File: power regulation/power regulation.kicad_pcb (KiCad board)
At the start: 4 copper layers, 175 x 100 mm, 90 parts, among them J1 Conn_01x02_Pin, J2 Conn_01x02_Pin, J3 Conn_01x02_Pin, M1 TO-236AB_SOT23_NEX, M2 TO-236AB_SOT23_NEX, U1 LT8640SEV_PBF, U2 LT8640SEV_PBF, U3 LT8619EDD-TRPBF

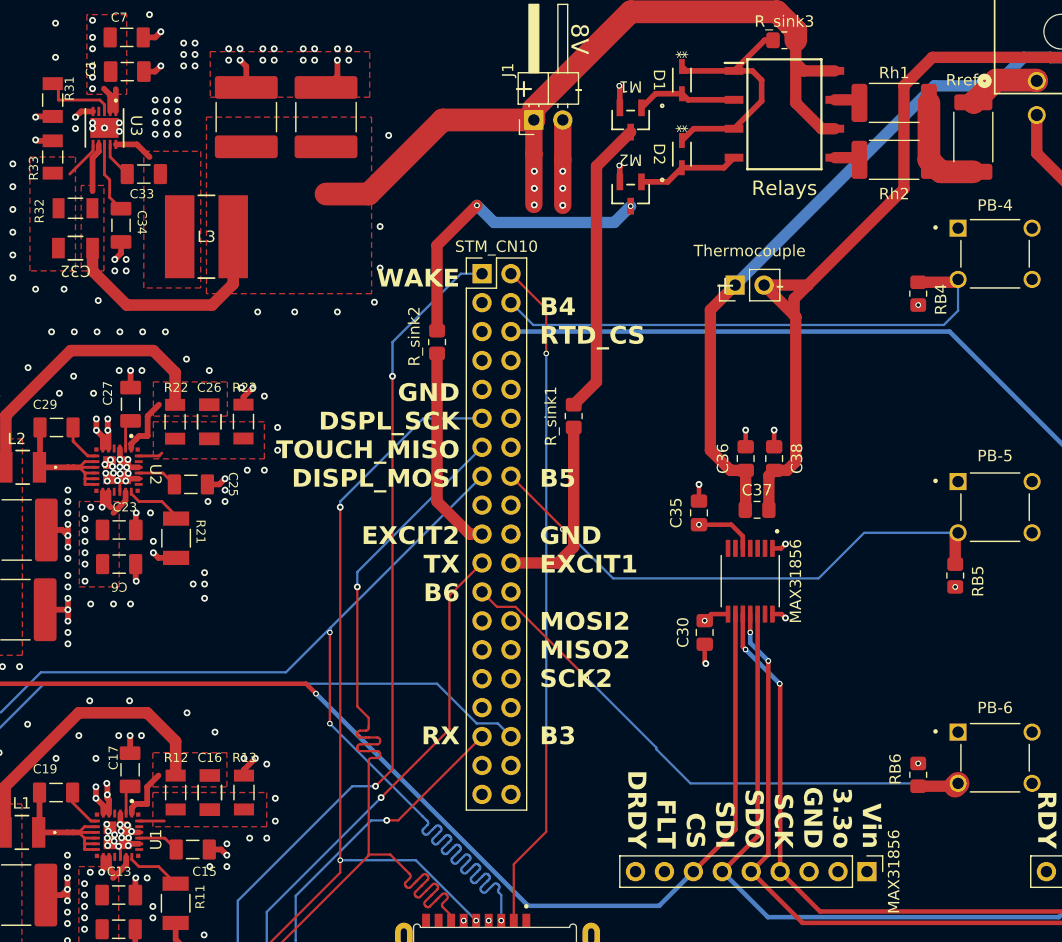
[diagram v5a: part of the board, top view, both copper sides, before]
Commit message: Change trace thickness to comply with tolerances.
Some of the ics might not work.
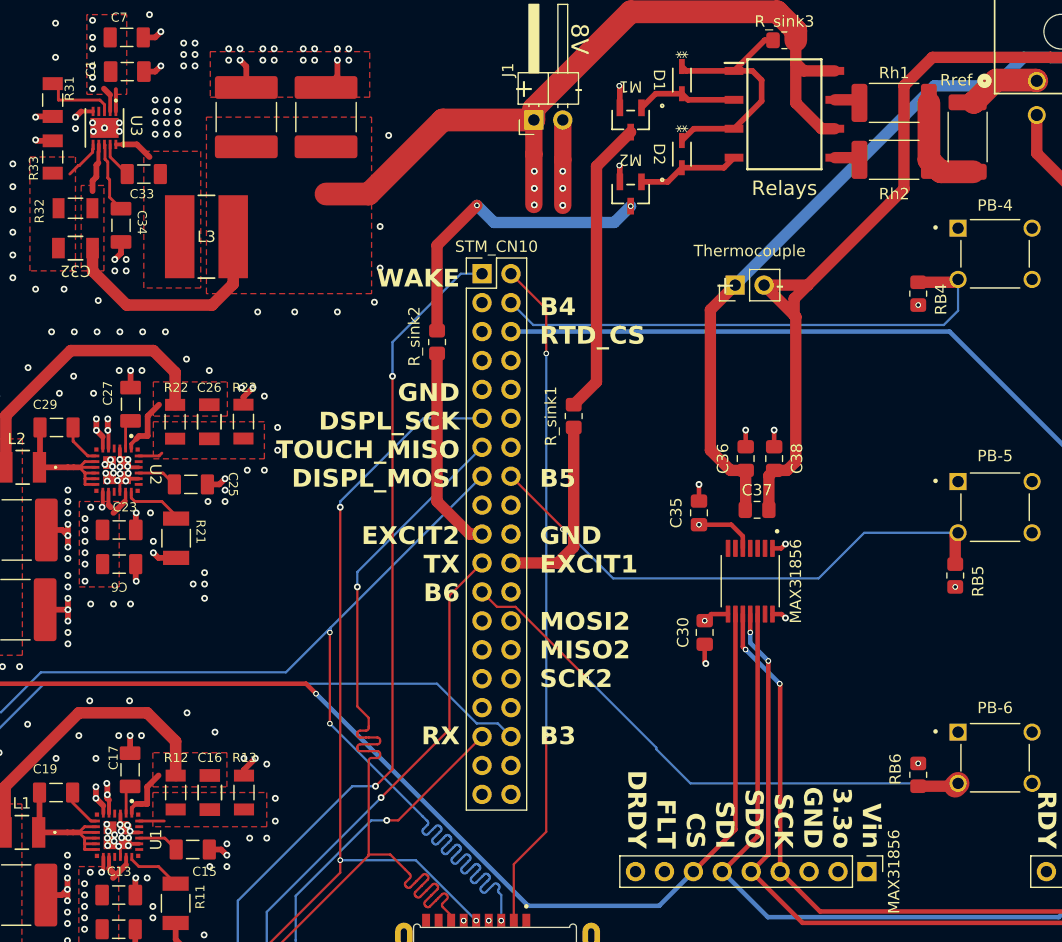
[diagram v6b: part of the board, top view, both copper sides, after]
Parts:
- moved Rref 0.50 mm to (206.5, 56.5)
